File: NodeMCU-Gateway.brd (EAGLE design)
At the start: 59.7 x 40.6 mm, 25 parts, among them J2 GROVE-I2C, J3 Lipo Battery, J4 GROVE-I2C, J5 CON_HEADER_1X08-PTH, P1 PADSMALL, P2 PADNORMAL

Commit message: Version 1.1
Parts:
- removed SJ1: JUMPER, SparkFun-Passives:PAD-JUMPER-2-NO_YES_SILK
- added R3: 10K, _c2h:0805-RES
- added SJPWR: (no value), SparkFun-Passives:PAD-JUMPER-3-NO_YES_SILK
- WS2812-1: device _c2h:WS2812B-LONG -> _c2h:WS2812-PTH
- moved LOGO1 40.7 mm to (18.0, 26.4)
- moved LOGO2 3.10 mm to (46.5, 25.8)
- moved RX-433MHZ 2.54 mm to (49.7, 39.9)
- moved P1 1.27 mm to (4.41, 4.92)
- moved U-FL 1.27 mm to (2.00, 4.92)
- moved C5 1.27 mm to (49.5, 3.17)
- moved C1 1.02 mm to (55.1, 30.5)
- moved SJLED 1.02 mm to (45.8, 3.81), turned to 270 degrees
- moved WS2812-1 0.97 mm to (55.9, 36.8), turned to 0 degrees
- moved P2 0.72 mm to (56.4, 27.2)
- moved WS2812 0.68 mm to (55.9, 3.81)
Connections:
- new net N$1: P2.1, WS2812-1.4
- net 3V3: now also R3.2, SJLED.3; no longer SJLED.1
- net DIN-2: now also WS2812-1.1; no longer SJ1.2, WS2812-1.4
- net GPIO0: no longer SJ1.1
- net GPIO2: now also R3.1, U$2.SEL, U$3.NSS; no longer U$2.IRQ, U$3.DIO0
- net N$2: now also J5.4, SJPWR.2; no longer P2.1, WS2812-1.2
- net RST: now also SJPWR.3; no longer J5.4
- net SS: now also U$2.IRQ, U$3.DIO0; no longer U$2.SEL, U$3.NSS
- net VIN: now also SJLED.1, SJPWR.1; no longer SJLED.3
- net VLED: now also WS2812-1.2; no longer WS2812-1.1
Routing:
- net VIN: track 45.9 -> 82.9 mm, vias 0 -> 1
- net SS: track 43.4 -> 23.2 mm, vias 2 -> 0
- net RST: track 76.5 -> 58.4 mm
- net GND: track 4.13 -> 17.0 mm, vias 11 -> 16
- net N$1: track 0.00 -> 11.7 mm
- net GPIO0: track 108.5 -> 119.0 mm, vias 1 -> 3
- net MISO: track 36.5 -> 27.3 mm
- net N$2: track 13.1 -> 20.9 mm
- net ANT: track 16.5 -> 22.3 mm
- net VLED: track 49.5 -> 45.8 mm
- net DIN-2: track 36.1 -> 33.2 mm
- net GPIO2: track 20.1 -> 22.9 mm, vias 0 -> 1
- net 3V3: track 171.1 -> 173.7 mm
- net N$5: track 2.07 -> 0.00 mm
- net GPIO3: track 59.0 -> 58.4 mm
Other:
- board text added: "DOUT"
- board text added: "IO0"
- board text added: "NodeMCU Gateway V1.1 http://hallard.me"
- board text added: "RST IO0"
- board text removed: "5V"
- board text removed: "Ant"
- board text removed: "NodeMCU Gateway V1.0 http://hallard.me"
- board text removed: "WS2812 DOUT"

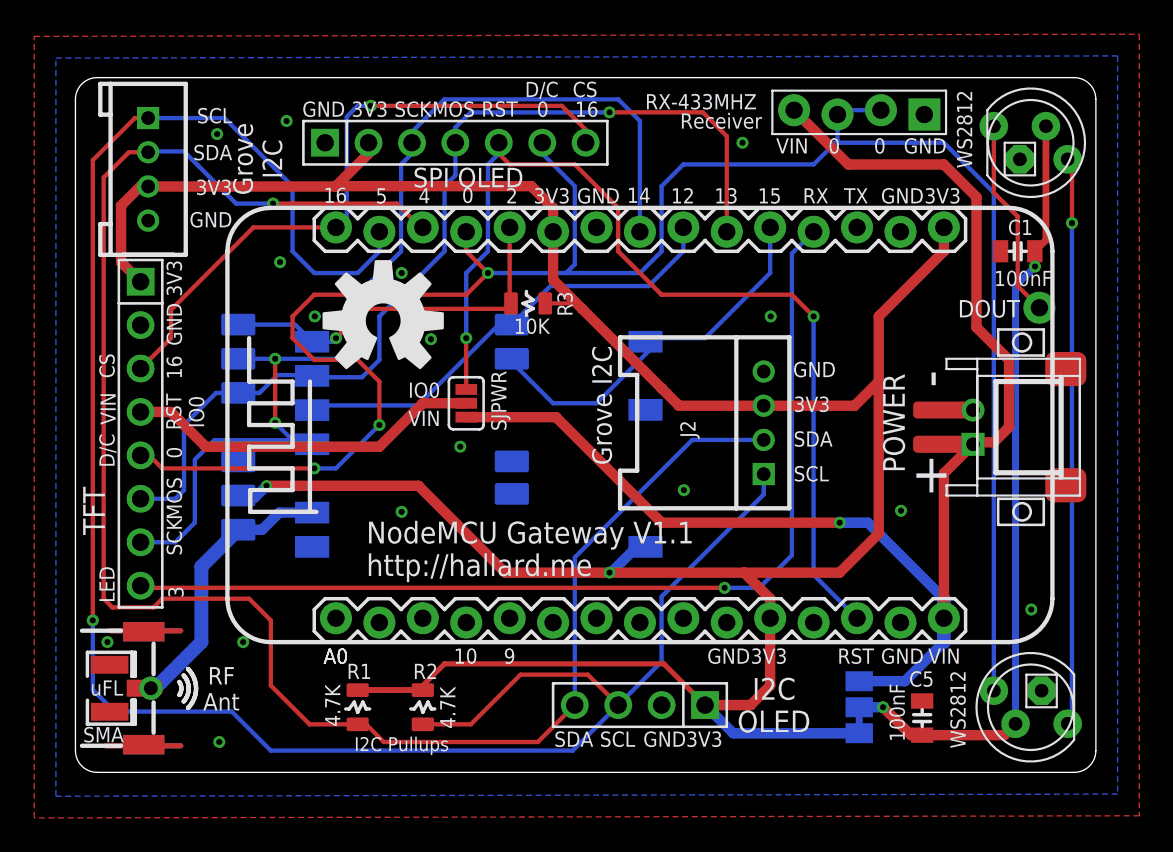
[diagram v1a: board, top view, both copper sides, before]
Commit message: Added Footprint for ATSHA204
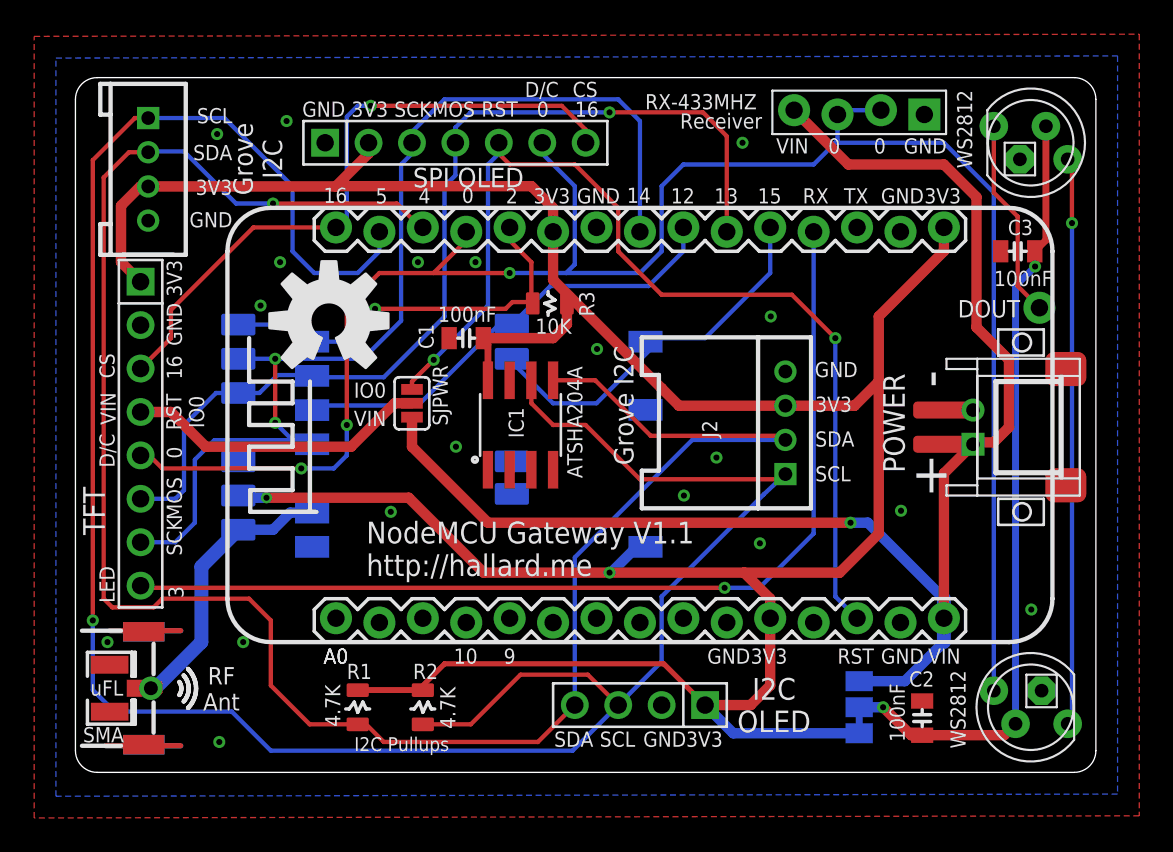
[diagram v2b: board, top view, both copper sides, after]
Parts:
- added C3: 100nF, _c2h:0805-CAP
- added IC1: ATSHA204A, SparkFun-DigitalIC:SOIC8
- moved C1 32.7 mm to (22.9, 25.4)
- moved LOGO1 3.18 mm to (14.8, 26.4)
- moved SJPWR 3.18 mm to (19.7, 21.6)
- moved J2 1.27 mm to (41.5, 20.4)
- moved R3 1.27 mm to (27.7, 27.4)
- moved LOGO2 0.90 mm to (47.1, 26.5)
- renumbered C5 to C2
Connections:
- net 3V3: now also C1.2, IC1.8
- net GND: now also C3.1, IC1.4
- net SCL: now also IC1.6
- net SDA: now also IC1.5
- net VLED: now also C3.2; no longer C1.2
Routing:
- net SCL: track 120.1 -> 138.9 mm
- net SDA: track 102.9 -> 119.2 mm
- net 3V3: track 173.7 -> 180.9 mm
- net GPIO0: track 119.0 -> 112.0 mm
- net VIN: track 82.9 -> 87.1 mm
- net N$2: track 20.9 -> 17.8 mm
- net RST: track 58.4 -> 59.7 mm
- net MOSI: track 57.5 -> 58.3 mm
- net GPIO2: track 22.9 -> 23.5 mm
- net GND: vias 16 -> 19

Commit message: Adjust SMA and UFL connectors
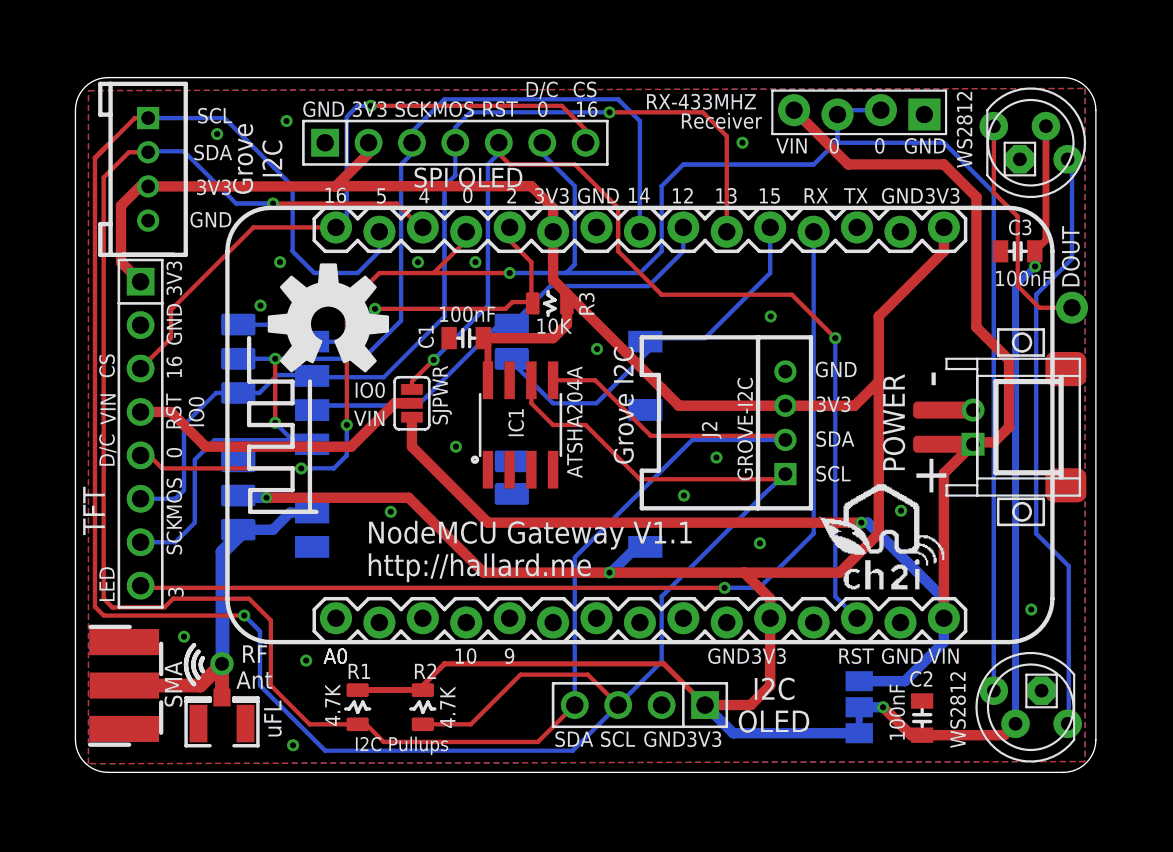
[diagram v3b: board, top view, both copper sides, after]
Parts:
- added J$1: SMA_EDGE, SparkFun-Connectors:SMA-EDGE
- added U$1, U$4: (no value), _c2h:LOGO_CH2I_75MM
- moved U-FL 6.89 mm to (8.57, 2.86), turned to 90 degrees
- moved P1 4.40 mm to (8.57, 6.35)
- moved P2 1.91 mm to (58.3, 27.2)
- moved LOGO1 0.19 mm to (14.8, 26.2)
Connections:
- net ANT: now also J$1.SIG
- net GND: now also J$1.GND@0, J$1.GND@1, J$1.GND@2, J$1.GND@3
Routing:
- net GND: track 17.0 -> 0.00 mm
- net N$1: track 11.7 -> 13.6 mm
- net DIN-2: track 33.2 -> 34.8 mm, vias 1 -> 0
- net SCL: track 138.9 -> 137.7 mm
- net ANT: track 22.3 -> 21.2 mm
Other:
- outline, holes or cut-outs redrawn

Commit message: Minor Silk Error
Silk SJPWR not tied to GPIO0 but RST/VIN
Increased SJPWR size for easy soldering
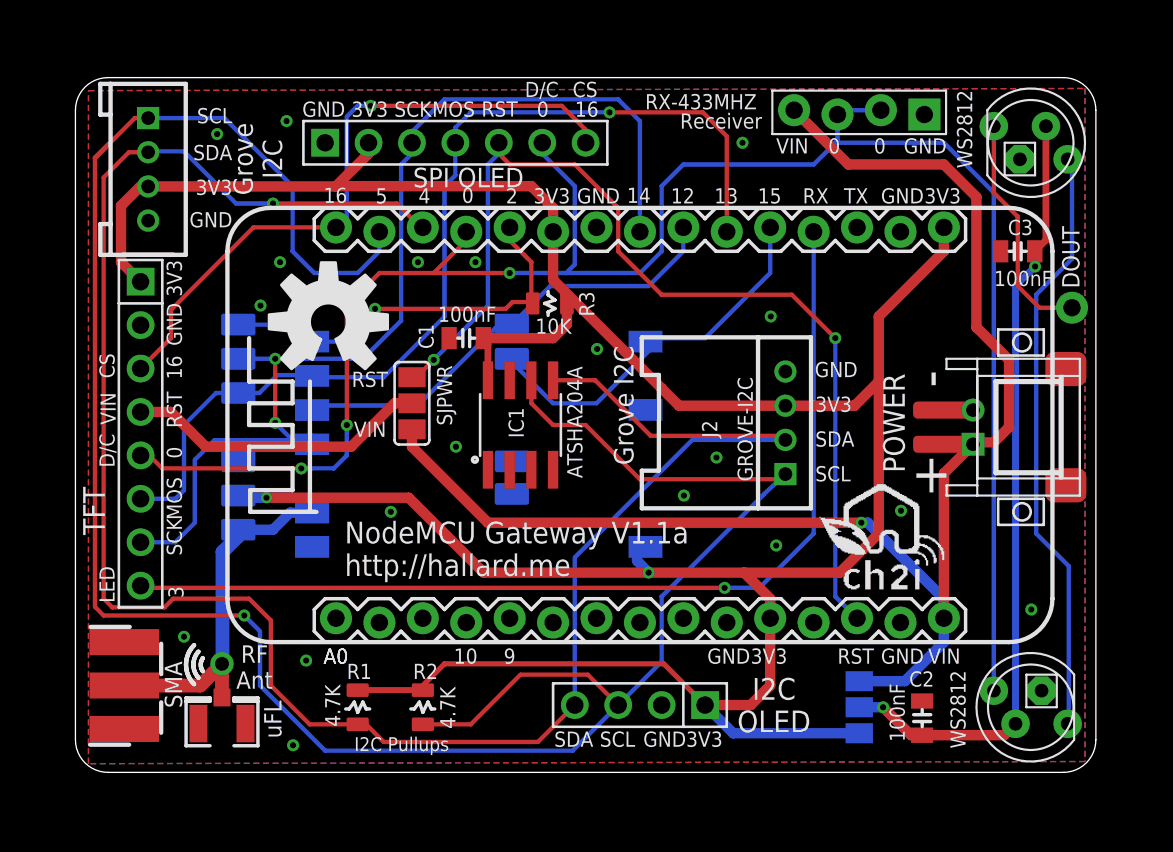
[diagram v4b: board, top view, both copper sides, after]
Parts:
- SJPWR: device SparkFun-Passives:PAD-JUMPER-3-NO_YES_SILK -> SparkFun-Passives:PAD-JUMPER-3-2OF3_NC_BY_TRACE_YES_SILK_LARGE
- moved LOGO1 0.13 mm to (14.8, 26.4)
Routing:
- net VIN: track 87.1 -> 86.4 mm
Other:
- board text added: "NodeMCU Gateway V1.1a http://hallard.me"
- board text removed: "IO0"
- board text removed: "NodeMCU Gateway V1.1 http://hallard.me"
- board text removed: "RST IO0"

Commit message: Version 1.2
Added FET to protect in case of power reverse, this avoid burning
NodeMCU board
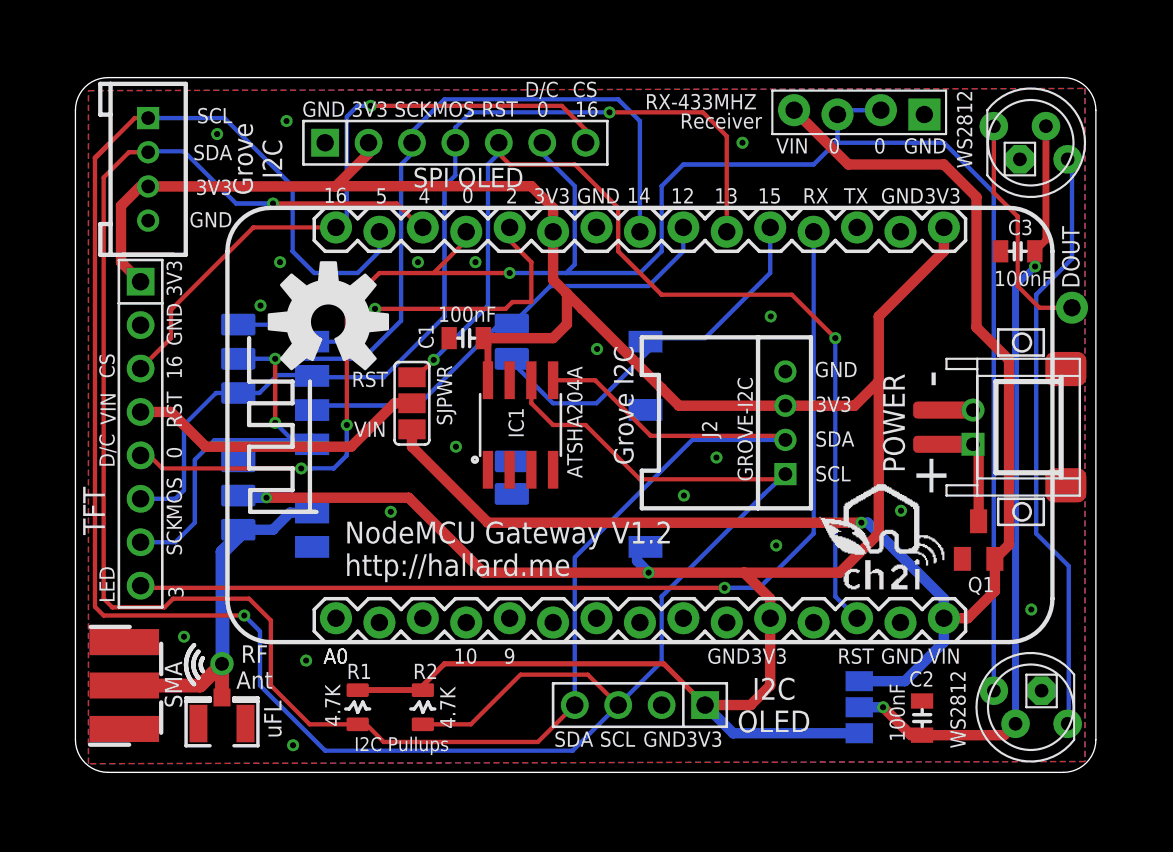
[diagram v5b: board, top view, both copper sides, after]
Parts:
- removed R3: 10K, _c2h:0805-RES
- added Q1: BSS84, transistor-small-signal:SOT23
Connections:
- new net PWR: J3.1, POWER.+, Q1.3
- net 3V3: no longer R3.2
- net GND: now also Q1.1
- net GPIO2: no longer R3.1
- net VIN: now also Q1.2; no longer J3.1, POWER.+
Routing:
- net PWR: track 0.00 -> 6.34 mm
- net VIN: track 86.4 -> 84.8 mm
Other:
- board text added: "NodeMCU Gateway V1.2 http://hallard.me"
- board text added: "VIN <=5V"
- board text removed: "NodeMCU Gateway V1.1a http://hallard.me"

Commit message: Bump to V1.3
* SMA/UFL Antenna connector has been size reduced
* Antenna trace and RF Module surrounded with via for better RF
isolation
* I2C OLED connector is now "lock" version, you can just plug to test it
will fit without connector
* No more LED solder pad to choose VIN/3V3, added 1N4148 diode from 5V
for the 1st LED to decrease VCC to 4.4V, always works
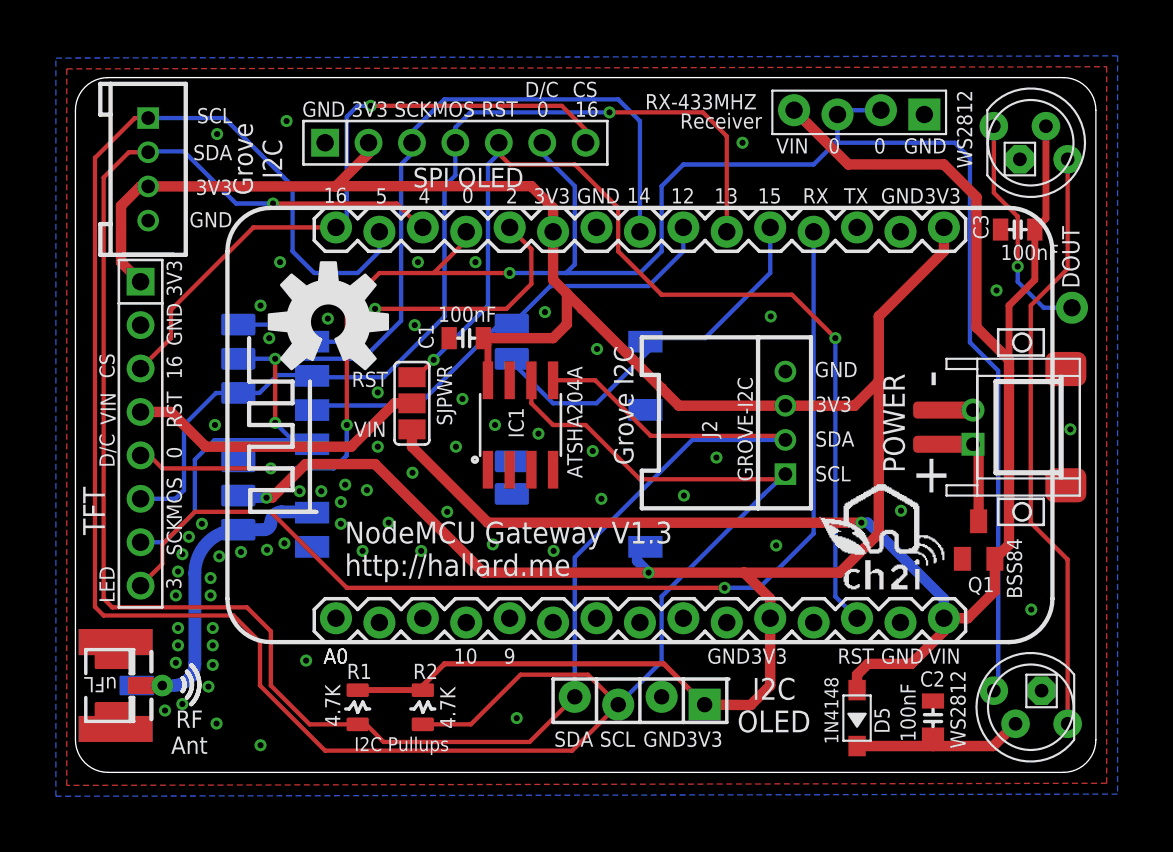
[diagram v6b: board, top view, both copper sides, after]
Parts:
- removed J$1: SMA_EDGE, SparkFun-Connectors:SMA-EDGE
- removed P1: PADSMALL, SteveMarple:PAD-SMALL
- removed SJLED: (no value), SparkFun-Passives:PAD-JUMPER-3-2OF3_NC_BY_TRACE_YES_SILK_LARGE
- removed U-FL: (no value), microbuilder:U.FL
- added D5: 1N4148, Seeed-Discrete:SOD123-2.7X1.6
- added J$2: ANTENNATINY, _c2h:SMA_UFL_PAD_TINY
- I2C_OLED: value CON_HEADER_1X04'SMALL'' -> CON_HEADER_1X04'LOCK'; device _c2h:M1X4 -> _c2h:1X04_LOCK
- moved I2C_OLED 5.27 mm to (38.1, 5.33)
- moved C3 1.27 mm to (55.1, 31.8)
- moved C2 0.63 mm to (50.2, 3.17)
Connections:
- removed net VLED: C2.2, C3.2, SJLED.2, WS2812-1.2, WS2812.2
- new net N$3: C2.2, D5.2, WS2812.2
- net 3V3: no longer SJLED.3
- net ANT: now also J$2.ANT1, J$2.ANT2, J$2.ANT3; no longer J$1.SIG, P1.1, U-FL.3
- net GND: now also J$2.GND1, J$2.GND2, J$2.GND3, J$2.GND4; no longer J$1.GND@0, J$1.GND@1, J$1.GND@2, J$1.GND@3, U-FL.1, U-FL.2
- net VIN: now also C3.2, D5.1, WS2812-1.2; no longer SJLED.1
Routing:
- net VLED: track 45.8 -> 0.00 mm, vias 2 -> 0
- net VIN: track 84.8 -> 100.5 mm
- net N$3: track 0.00 -> 10.4 mm
- net 3V3: track 180.5 -> 172.4 mm
- net GPIO3: track 58.4 -> 62.6 mm
- net ANT: track 21.2 -> 18.8 mm
- net SDA: track 119.2 -> 118.1 mm
- net GPIO2: track 23.4 -> 22.8 mm
- net GPIO0: track 112.0 -> 112.6 mm
- net SCL: track 137.7 -> 137.3 mm, vias 1 -> 0
- net N$1: track 13.6 -> 13.5 mm, vias 0 -> 1
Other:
- board text added: "NodeMCU Gateway V1.3 http://hallard.me"
- board text removed: "NodeMCU Gateway V1.2 http://hallard.me"
- board text removed: "SMA"
- board text removed: "VIN <=5V"
- board text removed: "uFL"
